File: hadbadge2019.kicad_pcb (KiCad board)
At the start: 4 copper layers, 88 x 137.5 mm, 149 parts, among them J1 Conn_02x04_Odd_Even, J10 Conn_01x02_Male, J11 Conn_02x06_Odd_Even, J2 USB_B_Micro, J3 Conn_01x02, J4 HDMI_A_1.4, J5 FH26W-45S-0.3SHW(60), J6 Conn_02x20_Odd_Even, J7 Conn_02x03_Odd_Even, J8 Conn_02x03_Odd_Even, J9 Conn_01x02_Male, Q1 AO3400, SW1 Up, SW2 Down, SW3 Left, SW4 Right, SW5 A, SW6 B, SW7 Select, SW8 Start, SW9 SW_SPDT_shielded, U1 LFE5Ux-45F, U10 NS8002, U2 LY68L6400SLIT, U3 LY68L6400SLIT, U4 W25Q128JVSIQ, U5 M3406, U6 XC6206P25, U7 XR1151, U9 XR1151, X1 X1G004481001400

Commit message: Proto2, final version
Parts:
- added C28: 100n, Capacitor_SMD:C_0603_1608Metric, B.Cu at (108.8, 107.9)
- added C29: 100n, Capacitor_SMD:C_0603_1608Metric, B.Cu at (105.8, 114.8)
- added C30: 10n, Capacitor_SMD:C_0603_1608Metric, B.Cu at (124.7, 128.8)
- added C48: 100n, Capacitor_SMD:C_0603_1608Metric, B.Cu at (135.8, 140.9)
- added D11: LED, LED_SMD:LED_0603_1608Metric, F.Cu at (145.8, 125.8)
- added D12: LED, LED_SMD:LED_0603_1608Metric, F.Cu at (147.2, 124.4)
- added D13: LED, LED_SMD:LED_0603_1608Metric, F.Cu at (148.6, 123.0)
- added D14: LED, LED_SMD:LED_0603_1608Metric, F.Cu at (150.0, 121.6)
- added D15: LED, LED_SMD:LED_0603_1608Metric, F.Cu at (151.4, 120.2)
- added R55: 4K7, Resistor_SMD:R_0603_1608Metric, B.Cu at (105.9, 108.6)
- added R56: 4K7, Resistor_SMD:R_0603_1608Metric, B.Cu at (101.9, 108.2)
- added R57: 100, Resistor_SMD:R_0603_1608Metric, B.Cu at (124.7, 130.4)
- added R58: 100K, Resistor_SMD:R_0603_1608Metric, B.Cu at (135.8, 137.8)
- added R59: 100K, Resistor_SMD:R_0603_1608Metric, B.Cu at (135.8, 139.3)
- added R60: NS, Resistor_SMD:R_0603_1608Metric, B.Cu at (137.6, 122.0)
- added R61: 470, Resistor_SMD:R_0603_1608Metric, B.Cu at (137.6, 125.2)
- added R62: 470, Resistor_SMD:R_0603_1608Metric, B.Cu at (137.4, 118.4)
- added R63: 470, Resistor_SMD:R_0603_1608Metric, B.Cu at (136.4, 133.4)
- added R64: 470, Resistor_SMD:R_0603_1608Metric, B.Cu at (136.4, 131.8)
- added R65: 470, Resistor_SMD:R_0603_1608Metric, B.Cu at (136.4, 130.2)
- added TP1: TestPoint, TestPoint:TestPoint_Pad_D1.0mm, B.Cu at (105.5, 145.1)
- added TP2: TestPoint, TestPoint:TestPoint_Pad_D1.0mm, B.Cu at (105.6, 152.5)
- added TP3: TestPoint, TestPoint:TestPoint_Pad_D1.0mm, B.Cu at (108.2, 147.3)
- added TP4: TestPoint, TestPoint:TestPoint_Pad_D1.0mm, B.Cu at (110.2, 147.2)
- added TP5: TestPoint, TestPoint:TestPoint_Pad_D1.0mm, B.Cu at (109.3, 144.9)
- added TP6: TestPoint, TestPoint:TestPoint_Pad_D1.0mm, B.Cu at (113.5, 132.5)
- added U11: 74LVC1G175, Package_TO_SOT_SMD:SOT-23-6, B.Cu at (107.7, 112.2)
- added U8: 74LVC1G3157, Package_TO_SOT_SMD:SOT-23-6, B.Cu at (102.3, 112.2)
- D3, D4: value D_Zener -> 3V6; footprint Diode_SMD:D_0603_1608Metric -> Diode_SMD:D_SOD-323
- J1: value Conn_02x04_Odd_Even -> Conn_02x05_Odd_Even; footprint Connector_PinHeader_2.54mm:PinHeader_2x04_P2.54mm_Vertical -> Connector_PinHeader_2.54mm:PinHeader_2x05_P2.54mm_Vertical
- moved J1 2.65 mm to (103.4, 150.4)
- moved C5 0.75 mm to (103.3, 154.6)
- moved X1 0.45 mm to (98.1, 154.9)
- moved C18 0.34 mm to (109.5, 142.1)
- moved C6 0.18 mm to (111.8, 140.6)
- moved D3 0.10 mm to (83.2, 85.2)
- turned R7 to 90 degrees
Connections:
- J1 pad 1: GND -> VBAT_ALWON
- J1 pad 2: VBAT_ALWON -> GND
- J1 pad 3: (no net) -> VIO
- J1 pad 4: VIO -> (no net)
- R1 pad 2: Net-(J1-Pad6) -> Net-(J1-Pad7)
- R2 pad 2: Net-(J1-Pad8) -> Net-(J1-Pad5)
- R3 pad 2: Net-(J1-Pad5) -> Net-(J1-Pad6)
- R4 pad 1: Net-(J1-Pad7) -> Net-(J1-Pad8)
- R48 pad 2: (no net) -> FLASH_CS_EXT
- R5 pad 2: (no net) -> PWMOUT
- R7 pad 1: /FPGA/FLASH_CS -> VIO
- R7 pad 2: VIO -> /FPGA/FLASH_CS_INT
- U1 pad A12: (no net) -> GENIO_28
- U1 pad A13: GENIO_28 -> PMODB_3
- U1 pad A14: PMODB_4 -> PMODA_3
- U1 pad A15: PMODA_3 -> PMODA_1
- U1 pad A16: PMODA_1 -> SAO2_SCL
- U1 pad A17: SAO2_SCL -> SAO2_GPIO2
- U1 pad A18: SAO2_GPIO2 -> LED9
- U1 pad A19: (no net) -> ADCREFOUT
- U1 pad B12: (no net) -> GENIO_27
- U1 pad B13: GENIO_27 -> PMODB_4
- U1 pad B15: PMODB_3 -> PMODB_1
- U1 pad B16: PMODB_1 -> SAO2_GPIO3
- U1 pad B17: SAO2_GPIO3 -> SAO2_SDA
- U1 pad B18: SAO2_SDA -> SAO2_GPIO1
- U1 pad B19: SAO2_GPIO1 -> LED8
- U1 pad B20: (no net) -> LED7
- U1 pad C12: (no net) -> Net-(TP6-Pad1)
- U1 pad C13: GENIO_26 -> (no net)
- U1 pad C15: (no net) -> PMODB_2
- U1 pad C18: (no net) -> ADCREF
- U1 pad D13: GENIO_25 -> (no net)
- U1 pad D14: GENIO_29 -> (no net)
- U1 pad D15: PMODA_4 -> (no net)
- U1 pad D16: PMODB_2 -> PMODA_4
- U1 pad D18: (no net) -> ADCREF
- U1 pad D5: (no net) -> /FPGA/FSEL_D
- U1 pad E17: (no net) -> GENIO_29
- U1 pad E5: (no net) -> /FPGA/FSEL_C
- U1 pad F17: (no net) -> ADCREF
- U1 pad G18: (no net) -> GENIO_25
- U1 pad H17: (no net) -> GENIO_26
- U1 pad H18: (no net) -> ADCREF
- U1 pad R5: Net-(J1-Pad8) -> Net-(J1-Pad5)
- U1 pad T1: (no net) -> PWMOUT
- U1 pad T18: (no net) -> Net-(TP5-Pad1)
- U1 pad T5: Net-(J1-Pad7) -> Net-(J1-Pad8)
- U1 pad U1: (no net) -> DBGTX
- U1 pad U17: (no net) -> Net-(TP1-Pad1)
- U1 pad U18: (no net) -> CLK
- U1 pad U19: (no net) -> Net-(TP3-Pad1)
- U1 pad U2: (no net) -> DBGRX
- U1 pad U20: (no net) -> Net-(TP4-Pad1)
- U1 pad U5: Net-(J1-Pad6) -> Net-(J1-Pad7)
- U1 pad V4: Net-(J1-Pad5) -> Net-(J1-Pad6)
- U4 pad 1: (no net) -> /FPGA/FLASH_CS_INT
- X1 pad 3: (no net) -> CLK
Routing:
- net (no net): track 49.3 -> 0.00 mm, vias 3 -> 0
- net /FPGA/FLASH_CS_INT: track 0.00 -> 42.8 mm, vias 0 -> 4
- net PWMOUT: track 0.00 -> 31.8 mm, vias 0 -> 3
- net VIO: track 70.7 -> 96.4 mm, vias 18 -> 20
- net Net-(D14-Pad2): track 0.00 -> 24.4 mm, vias 0 -> 3
- net Net-(D15-Pad2): track 0.00 -> 21.0 mm, vias 0 -> 1
- net VBAT: track 213.7 -> 234.5 mm
- net /FPGA/FSEL_C: track 0.00 -> 20.6 mm, vias 0 -> 1
- net Net-(D13-Pad2): track 0.00 -> 20.2 mm, vias 0 -> 1
- net CLK: track 0.00 -> 19.9 mm, vias 0 -> 1
- net LED8: track 0.00 -> 19.4 mm, vias 0 -> 1
- net LED9: track 0.00 -> 19.3 mm, vias 0 -> 1
- net LED7: track 0.00 -> 19.0 mm, vias 0 -> 1
- net GND: track 244.7 -> 263.0 mm, vias 81 -> 91
- net Net-(D12-Pad2): track 0.00 -> 17.0 mm, vias 0 -> 1
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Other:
- board text added: "...What are you doing, reading this text? Please put the display back, there's nothing interesting under it, except for a few traces and this text."
- board text added: "HACK -O- METER"
- board text added: "Hackaday Supercon 2019 Badge Proto v2 If you have this, you are super-l33t, and/or get to suffer through all the bugs that the final version won't have."
- board text added: "Hello there. Trying to find R61 perhaps? Good luck!"
- board text added: "J1: VBAT GND 3V3 KEY TDI TDO TMS TCK TX RX"
- board text added: "J6: GND 3V3 F_HOLD F_CS F_SCK F_MISO F_MOSI F_WP GENIO2 GENIO1 GENIO4 GENIO3 ..... GENIO30 GENIO29 5V VBAT"
- board text removed: "8/16MB RAM"
- board text removed: "GND VIO IO2 IO1 IO4 IO3 ETC"
- board text removed: "Hackaday Supercon 2019 Badge Proto v2 Spritesmods.com"
- board text removed: "JTAG: GND VBAT NC VIO TDO TMS TCK TDI"

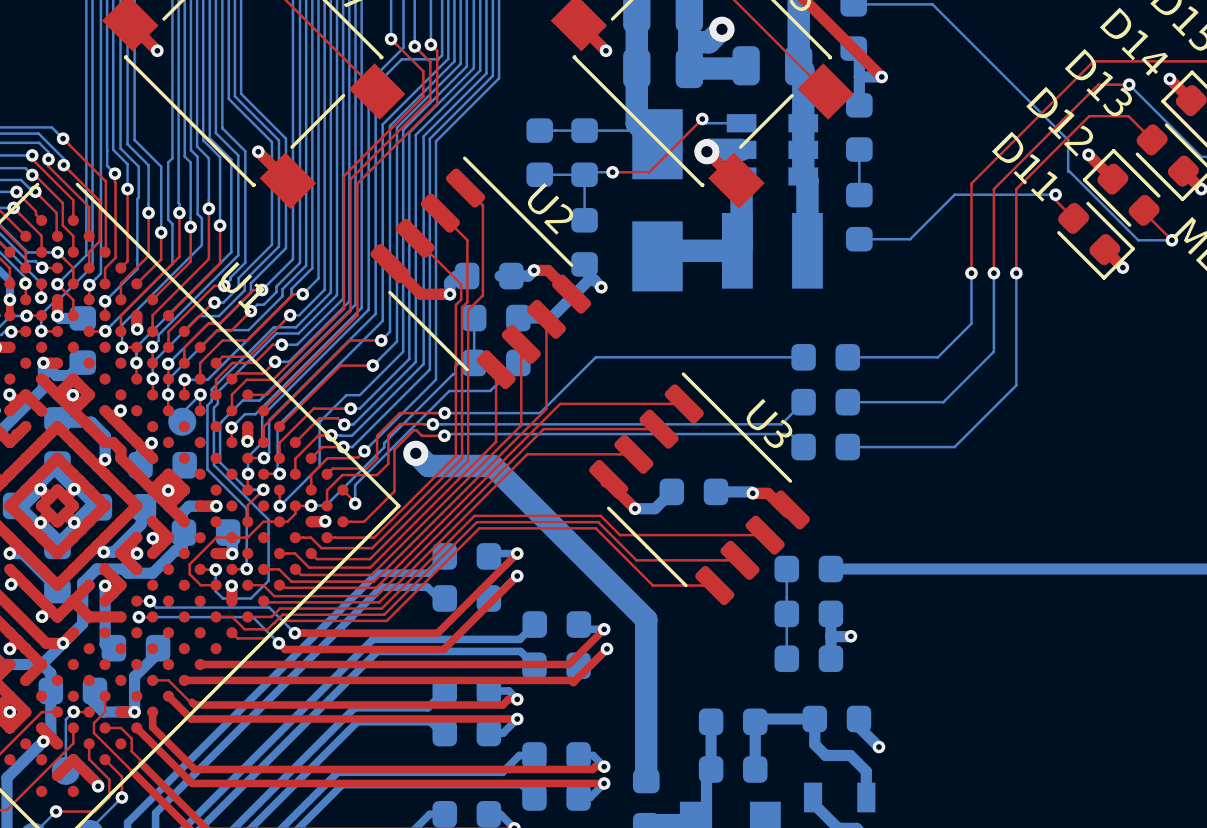
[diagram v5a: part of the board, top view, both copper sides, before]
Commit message: Fix fab drawings to make sense
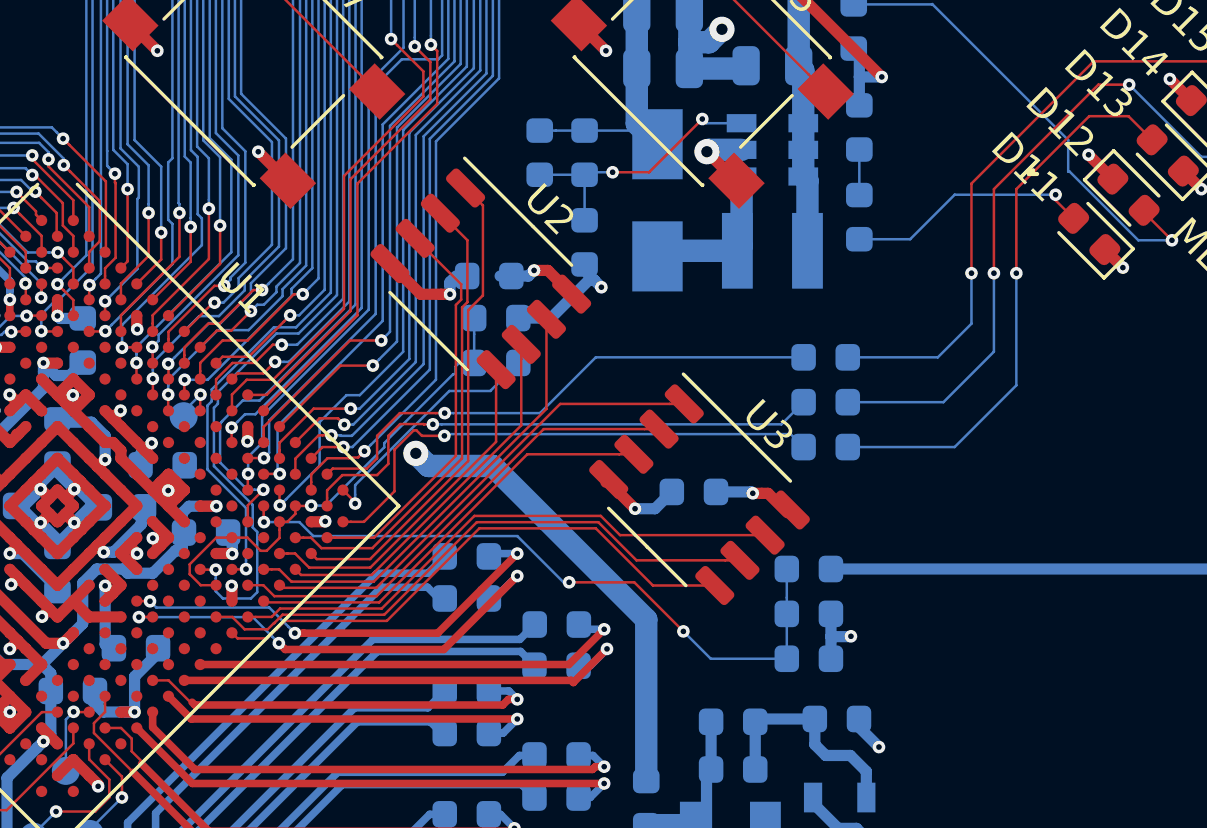
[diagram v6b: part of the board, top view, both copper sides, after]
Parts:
- D10, D11, D5, D8: value LED -> LED RED
- D12, D13, D6, D7, D9: value LED -> LED YELLOW
- D14, D15: value LED -> LED GREEN
- J3: value Conn_01x02 -> NO STUFF
- moved J4 6.00 mm to (116.0, 155.5)
- moved TP6 0.21 mm to (113.5, 132.3)
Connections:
- C48 pad 1: ADC1 -> ADC4
- R58 pad 2: ADC1 -> ADC4
- R59 pad 1: ADC1 -> ADC4
- U1 pad D17: (no net) -> ADC4
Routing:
- net ADC4: track 0.00 -> 24.4 mm, vias 0 -> 3
- net ADC1: track 3.20 -> 0.00 mm
- net ADCREF: track 16.6 -> 17.3 mm

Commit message: No idea what these tiny differences are... Done with proto 2, prepare for proto 3!
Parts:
- J11: value Conn_02x06_Odd_Even -> NO STUFF
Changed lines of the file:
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@@
       (padsonsilk false)
       (subtractmaskfromsilk false)
-      (outputformat 4)
+      (outputformat 1)
       (mirror false)
       (drillshape 0)
@@
     (add_net "Net-(D8-Pad2)")
     (add_net "Net-(D9-Pad2)")
+    (add_net "Net-(J1-Pad4)")
     (add_net "Net-(J1-Pad5)")
     (add_net "Net-(J1-Pad6)")
@@
     (add_net "Net-(R54-Pad1)")
     (add_net "Net-(R60-Pad2)")
+    (add_net "Net-(SW9-Pad3)")
     (add_net "Net-(TP1-Pad1)")
     (add_net "Net-(TP11-Pad1)")
@@
     (add_net "Net-(TP5-Pad1)")
     (add_net "Net-(TP6-Pad1)")
+    (add_net "Net-(U1-PadC13)")
+    (add_net "Net-(U1-PadD12)")
+    (add_net "Net-(U1-PadD13)")
+    (add_net "Net-(U1-PadD14)")
+    (add_net "Net-(U1-PadD15)")
+    (add_net "Net-(U1-PadD7)")
+    (add_net "Net-(U1-PadD8)")
+    (add_net "Net-(U1-PadE10)")
+    (add_net "Net-(U1-PadE11)")
+    (add_net "Net-(U1-PadE12)")
+    (add_net "Net-(U1-PadE13)")
+    (add_net "Net-(U1-PadE14)")
+    (add_net "Net-(U1-PadE15)")
+    (add_net "Net-(U1-PadE16)")
+    (add_net "Net-(U1-PadE18)")
+    (add_net "Net-(U1-PadE6)")
+    (add_net "Net-(U1-PadE7)")
+    (add_net "Net-(U1-PadE8)")
+    (add_net "Net-(U1-PadE9)")
+    (add_net "Net-(U1-PadF16)")
+    (add_net "Net-(U1-PadF18)")
+    (add_net "Net-(U1-PadF5)")
+    (add_net "Net-(U1-PadG16)")
+    (add_net "Net-(U1-PadG5)")
+    (add_net "Net-(U1-PadH16)")
+    (add_net "Net-(U1-PadH3)")
+    (add_net "Net-(U1-PadH4)")
+    (add_net "Net-(U1-PadH5)")
+    (add_net "Net-(U1-PadJ16)")
+    (add_net "Net-(U1-PadJ17)")
+    (add_net "Net-(U1-PadJ18)")
+    (add_net "Net-(U1-PadJ5)")
+    (add_net "Net-(U1-PadK16)")
+    (add_net "Net-(U1-PadK17)")
+    (add_net "Net-(U1-PadK18)")
+    (add_net "Net-(U1-PadK19)")
+    (add_net "Net-(U1-PadK20)")
+    (add_net "Net-(U1-PadK5)")
+    (add_net "Net-(U1-PadL18)")
+    (add_net "Net-(U1-PadL19)")
+    (add_net "Net-(U1-PadL5)")
+    (add_net "Net-(U1-PadM17)")
+    (add_net "Net-(U1-PadM18)")
+    (add_net "Net-(U1-PadM19)")
+    (add_net "Net-(U1-PadM5)")
+    (add_net "Net-(U1-PadN16)")
+    (add_net "Net-(U1-PadN17)")
+    (add_net "Net-(U1-PadN18)")
+    (add_net "Net-(U1-PadN5)")
+    (add_net "Net-(U1-PadP16)")
+    (add_net "Net-(U1-PadP17)")
+    (add_net "Net-(U1-PadP18)")
+    (add_net "Net-(U1-PadP19)")
+    (add_net "Net-(U1-PadR16)")
+    (add_net "Net-(U1-PadR17)")
+    (add_net "Net-(U1-PadR3)")
+    (add_net "Net-(U1-PadT16)")
+    (add_net "Net-(U1-PadT17)")
+    (add_net "Net-(U1-PadT2)")
+    (add_net "Net-(U1-PadT20)")
+    (add_net "Net-(U1-PadT3)")
+    (add_net "Net-(U1-PadU16)")
+    (add_net "Net-(U1-PadV1)")
+    (add_net "Net-(U1-PadW10)")
+    (add_net "Net-(U1-PadW11)")
+    (add_net "Net-(U1-PadW13)")
+    (add_net "Net-(U1-PadW14)")
+    (add_net "Net-(U1-PadW17)")
+    (add_net "Net-(U1-PadW18)")
+    (add_net "Net-(U1-PadW20)")
+    (add_net "Net-(U1-PadW4)")
+    (add_net "Net-(U1-PadW5)")
+    (add_net "Net-(U1-PadW8)")
+    (add_net "Net-(U1-PadW9)")
+    (add_net "Net-(U1-PadY11)")
+    (add_net "Net-(U1-PadY12)")
+    (add_net "Net-(U1-PadY14)")
+    (add_net "Net-(U1-PadY15)")
+    (add_net "Net-(U1-PadY16)")
+    (add_net "Net-(U1-PadY17)")
+    (add_net "Net-(U1-PadY19)")
+    (add_net "Net-(U1-PadY5)")
+    (add_net "Net-(U1-PadY6)")
+    (add_net "Net-(U1-PadY7)")
+    (add_net "Net-(U1-PadY8)")
     (add_net "Net-(U11-Pad4)")
     (add_net PMODA_1)
@@
   (module lib:Murata_1212 (layer B.Cu)
     (at 133 147.4)
+    (attr smd)
     (fp_text reference L1 (at -2.8 1.05) (layer B.SilkS)
       (effects (font (size 1 1) (thickness 0.15)) (justify mirror))
@@
       (effects (font (size 1 1) (thickness 0.15)))
     )
-    (fp_text value Conn_02x06_Odd_Even (at 1.4 6.25) (layer F.Fab)
+    (fp_text value "NO STUFF" (at 1.4 6.25) (layer F.Fab)
       (effects (font (size 1 1) (thickness 0.15)))
     )
@@
   (module lib:Murata_1212 (layer B.Cu)
     (at 134.5 126.4)
+    (attr smd)
     (fp_text reference L3 (at -0.125 2.325) (layer B.SilkS)
       (effects (font (size 1 1) (thickness 0.15)) (justify mirror))
@@
   (module lib:Murata_1212 (layer B.Cu)
     (at 134.3 113.2)
+    (attr smd)
     (fp_text reference L2 (at 2.975 0.95) (layer B.SilkS)
       (effects (font (size 1 1) (thickness 0.15)) (justify mirror))

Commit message: This is proto 3.
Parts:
- added A1: art, lib:badge_art, F.Cu at (146.9, 147.9)
- added C49: 100n, Capacitor_SMD:C_0603_1608Metric, F.Cu at (124.5, 32.1)
- added C50: 10u, Capacitor_SMD:C_0805_2012Metric, F.Cu at (118.7, 33.9)
- added C51: 100n, Capacitor_SMD:C_0603_1608Metric, F.Cu at (118.7, 31.9)
- added J12: NO STUFF, Connector_PinHeader_2.54mm:PinHeader_1x04_P2.54mm_Vertical, B.Cu at (78.5, 82.3)
- added Q2: AO3401, Package_TO_SOT_SMD:SOT-23, B.Cu at (146.6, 102.3)
- added Q3: AO3400, Package_TO_SOT_SMD:SOT-23, B.Cu at (78.1, 53.4)
- added Q4: AO3400, Package_TO_SOT_SMD:SOT-23, B.Cu at (78.1, 58.8)
- added Q5: AO3400, Package_TO_SOT_SMD:SOT-23, B.Cu at (78.1, 64.2)
- added R66: 4K7, Resistor_SMD:R_0603_1608Metric, B.Cu at (108.2, 118.0)
- added R67: 4K7, Resistor_SMD:R_0603_1608Metric, B.Cu at (108.9, 105.1)
- added R68: 10K, Resistor_SMD:R_0603_1608Metric, B.Cu at (74.3, 82.0)
- added R69: 10K, Resistor_SMD:R_0603_1608Metric, B.Cu at (78.1, 56.0)
- added R70: 10K, Resistor_SMD:R_0603_1608Metric, B.Cu at (78.1, 61.4)
- added R71: 10K, Resistor_SMD:R_0603_1608Metric, B.Cu at (78.1, 66.9)
- added TP7: TestPoint, TestPoint:TestPoint_Pad_D1.0mm, B.Cu at (118.3, 138.3)
- added U12: RPM973, lib:RPM973-H11, F.Cu at (120.8, 28.7)
- D10, D11, D5, D8: value LED RED -> FC-B1010RGBT-HG; footprint LED_SMD:LED_0603_1608Metric -> lib:FC-B1010RGBT-HG
- D12, D13, D6, D7, D9: value LED YELLOW -> FC-B1010RGBT-HG; footprint LED_SMD:LED_0603_1608Metric -> lib:FC-B1010RGBT-HG
- D14, D15: value LED GREEN -> FC-B1010RGBT-HG; footprint LED_SMD:LED_0603_1608Metric -> lib:FC-B1010RGBT-HG
- R23: value 560K -> 750K
- R41, R42, R43, R44, R45, R46, R61, R62, R63, R64, R65: value 470 -> 220R
- R6: value 330K -> 360K
- X1: footprint Crystal:Crystal_SMD_7050-4Pin_7.0x5.0mm -> lib:Seiko_fp_crystal_SMD_7050-4Pin_7.0x5.0mm
- moved R62 19.1 mm to (131.7, 136.6), turned to 0 degrees
- moved R60 17.5 mm to (132.0, 138.6), turned to 0 degrees
- moved R61 11.0 mm to (135.8, 136.1), turned to 0 degrees
- moved C30 8.53 mm to (132.9, 130.8), turned to 270 degrees
- moved R29 8.18 mm to (82.5, 86.0)
- moved R30 8.17 mm to (81.0, 86.0)
- moved R57 6.76 mm to (131.4, 130.8), turned to 270 degrees
- moved C47 5.84 mm to (97.8, 97.7), turned to 270 degrees
- moved J11 5.77 mm to (140.4, 33.0)
- moved R27 5.27 mm to (76.5, 87.7)
- moved R32 5.27 mm to (76.5, 86.1)
- moved C1 4.94 mm to (128.9, 129.3), turned to 0 degrees
- moved R25 4.11 mm to (87.2, 86.7)
- moved R23 3.86 mm to (128.7, 106.8), turned to 0 degrees
- moved R6 3.27 mm to (127.8, 120.0), turned to 90 degrees
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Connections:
- BT1 pad 1: VBAT_ALWON -> Net-(BT1-Pad1)
- D10 pad 1: GND -> Net-(D10-Pad1)
- D10 pad 2: Net-(D10-Pad2) -> CATR
- D11 pad 1: GND -> Net-(D11-Pad1)
- D11 pad 2: Net-(D11-Pad2) -> CATR
- D12 pad 1: GND -> Net-(D12-Pad1)
- D12 pad 2: Net-(D12-Pad2) -> CATR
- D13 pad 1: GND -> Net-(D13-Pad1)
- D13 pad 2: Net-(D13-Pad2) -> CATR
- D14 pad 1: GND -> Net-(D14-Pad1)
- D14 pad 2: Net-(D14-Pad2) -> CATR
- D15 pad 1: GND -> Net-(D15-Pad1)
- D15 pad 2: Net-(D15-Pad2) -> CATR
- D5 pad 1: GND -> Net-(D5-Pad1)
- D5 pad 2: Net-(D5-Pad2) -> CATR
- D6 pad 1: GND -> Net-(D6-Pad1)
- D6 pad 2: Net-(D6-Pad2) -> CATR
- D7 pad 1: GND -> Net-(D7-Pad1)
- D7 pad 2: Net-(D7-Pad2) -> CATR
- D8 pad 1: GND -> Net-(D8-Pad1)
- D8 pad 2: Net-(D8-Pad2) -> CATR
- D9 pad 1: GND -> Net-(D9-Pad1)
- D9 pad 2: Net-(D9-Pad2) -> CATR
- R41 pad 2: Net-(D5-Pad2) -> Net-(D5-Pad1)
- R42 pad 2: Net-(D6-Pad2) -> Net-(D6-Pad1)
- R43 pad 2: Net-(D7-Pad2) -> Net-(D7-Pad1)
- R44 pad 2: Net-(D8-Pad2) -> Net-(D8-Pad1)
- R45 pad 2: Net-(D9-Pad2) -> Net-(D9-Pad1)
- R46 pad 2: Net-(D10-Pad2) -> Net-(D10-Pad1)
- R60 pad 1: VIO -> LED10
- R61 pad 2: Net-(D11-Pad2) -> Net-(D11-Pad1)
- R62 pad 1: VIO -> LED11
- R62 pad 2: Net-(D12-Pad2) -> Net-(D12-Pad1)
- R63 pad 2: Net-(D13-Pad2) -> Net-(D13-Pad1)
- R64 pad 2: Net-(D14-Pad2) -> Net-(D14-Pad1)
- R65 pad 2: Net-(D15-Pad2) -> Net-(D15-Pad1)
- U1 pad J16: (no net) -> Net-(TP7-Pad1)
- U1 pad K18: (no net) -> LEDB
- U1 pad K19: (no net) -> LED11
- U1 pad K20: (no net) -> LED10
- U1 pad L18: (no net) -> LEDG
- U1 pad P19: (no net) -> LEDR
- U1 pad R16: (no net) -> IRDA_TX
- U1 pad T16: (no net) -> IRDA_SD
- U1 pad U16: (no net) -> IRDA_RX
- U8 pad 1: /FPGA/FLASH_CS_INT -> FLASH_CS_EXT
- U8 pad 3: FLASH_CS_EXT -> /FPGA/FLASH_CS_INT
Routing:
- net CATB: track 0.00 -> 191.9 mm, vias 0 -> 4
- net CATR: track 0.00 -> 182.4 mm, vias 0 -> 6
- net CATG: track 0.00 -> 180.4 mm, vias 0 -> 16
- net IRDA_SD: track 0.00 -> 163.7 mm, vias 0 -> 5
- net IRDA_TX: track 0.00 -> 159.7 mm, vias 0 -> 4
- net IRDA_RX: track 0.00 -> 156.0 mm, vias 0 -> 2
- net LEDR: track 0.00 -> 150.8 mm, vias 0 -> 3
- net LEDG: track 0.00 -> 148.5 mm, vias 0 -> 3
- net LEDB: track 0.00 -> 141.6 mm, vias 0 -> 3
- net VBAT: track 234.5 -> 306.6 mm, vias 2 -> 3
- net GND: track 263.0 -> 327.9 mm, vias 91 -> 85
- net Net-(BT1-Pad2): track 67.8 -> 126.7 mm
- net Net-(D12-Pad1): track 0.00 -> 26.7 mm, vias 0 -> 1
- net Net-(D14-Pad2): track 24.4 -> 0.00 mm, vias 3 -> 0
- net /FPGA/FLASH_CS: track 31.0 -> 54.6 mm
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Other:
- board size 88 x 137.5 mm -> 88 x 140.5 mm
- board text added: "...HOW DID YOU REMOVE THIS?"
- board text added: "...What are you doing, reading this text? Please put the display back, there's nothing interesting under it, except for a few traces and these silkscreen scribbles. Oh, and the back of J12. Hope you don't need that one."
- board text added: "...YOU BRUTE"
- board text added: "D5-D10: GENERAL PURPOSE MULTI-WAVELENGTH PHOTONIC INDICATORS"
- board text added: "DRM GPIO3"
- board text added: "HELLO THERE. TRYING TO SOLDER R60? GOOD LUCK!"
- board text added: "Hackaday Supercon 2019 Badge Proto v3 If you have this, you are hyper-l33t, and/or get to suffer through the last few bugs that the final version won't have."
- board text added: "J11: PMOD 3V3 3V3 GND GND PMODA1 PMODB1 PMODA2 PMODB2 PMODA3 PMODB3 PMODA4 PMODB4"
- board text added: "J12: RED WHITE GREEN BLACK"
- board text added: "J4: WE-CAN'T-OFFICIALLY-CALL-IT-HDMI CONNECTOR"
- board text added: "J6: CARTRIDGE CONNECTOR GND 3V3 F_HOLD F_CS F_SCK F_MISO F_MOSI F_WP GENIO2 GENIO1 GENIO4 GENIO3 ..... GENIO30 GENIO29 5V VBAT"
- board text added: "J8-J11: SAO V1.69 BIS X-TREME! HDRS GPIO1 GPIO2 SDA SCL GND 3V3"
- board text added: "LY1"
- board text added: "LY1: YOUR LANYARD GOES HERE. OBVIOUSLY."
- board text added: "ON"
- board text added: "SOOO, ARE YOU GOING TO DISMANTLE THE ENTIRE BADGE, OR DO YOU JUST HATE AA BATTERY HOLDERS?"
- board text added: "U12: FIR IRDA TRANSCEIVER (SO BADGES CAN BLINK INTENSLY AT EACHOTHER)"
- board text added: "YOUR AD HERE? SEND AN EMAIL TO JEROEN@SPRITESMODS.COM"
- board text removed: "...What are you doing, reading this text? Please put the display back, there's nothing interesting under it, except for a few traces and this text."
- board text removed: "Hackaday Supercon 2019 Badge Proto v2 If you have this, you are super-l33t, and/or get to suffer through all the bugs that the final version won't have."
- board text removed: "Hello there. Trying to find R61 perhaps? Good luck!"
- board text removed: "J6: GND 3V3 F_HOLD F_CS F_SCK F_MISO F_MOSI F_WP GENIO2 GENIO1 GENIO4 GENIO3 ..... GENIO30 GENIO29 5V VBAT"
- board text removed: "ON ->"
- board text removed: "SAO: shroud space?"
